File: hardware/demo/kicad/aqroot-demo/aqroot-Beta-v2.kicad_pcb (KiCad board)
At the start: 6 copper layers, 72 x 148 mm, 311 parts, among them J1 FH69-50S-0.5SH, J2 Molex_5025700893, J3 USB_C_Receptacle_USB2.0_16P, J4 JST-PH-2 BATTERY, J5 COMMUNITY_PORT_1x24, J6 JST-PH-2 SPEAKER, J7 BM02B-ACHSS-GAN-ETF, J8 QWIIC_STEMMA_QT, Q1 AO3400A, Q10 2N7002, Q2 NTMD4820N, Q3 NTMD4820N, Q4 BSS138, Q5 AO3401A, Q6 BSS138, Q7 BSS138, Q8 BSS138, Q9 BSS138, SW1 BOOT, SW2 UP, SW3 DOWN, SW4 LEFT, SW5 RIGHT, SW6 A_SELECT, SW7 B_BACK, SW9 SW_SPDT, U1 ESP32-S3-WROOM-1, U10 USBLC6-2SC6, U11 BQ25185, U12 TPS63020, U13 TPS61023, U14 MAX17048, U16 TCA4307DGKR, U17 TPS61169DCKR, U18 LTC4368-1, U19 TLV7032, U2 PCAL9535APW, U20 TPS22950C, U21 TPS61023, U22 TPS22950C, U3 PCAL9535APW, U4 BMI270, U5 MAX98357A, U6 TSOP38238, U7 E07-400M10S, U8 E22-900M22S, U9 ST25R3916-AQET, Y1 27.12MHz 10pF 3225-4P

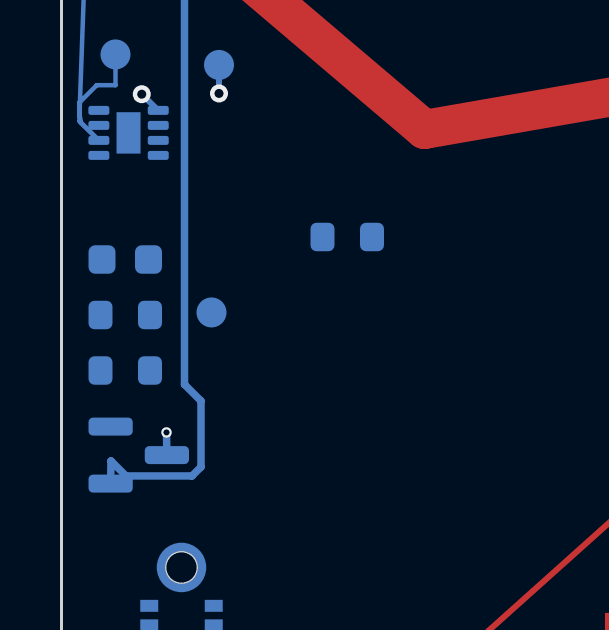
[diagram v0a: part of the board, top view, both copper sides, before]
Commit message: demo: route VBUS present tree
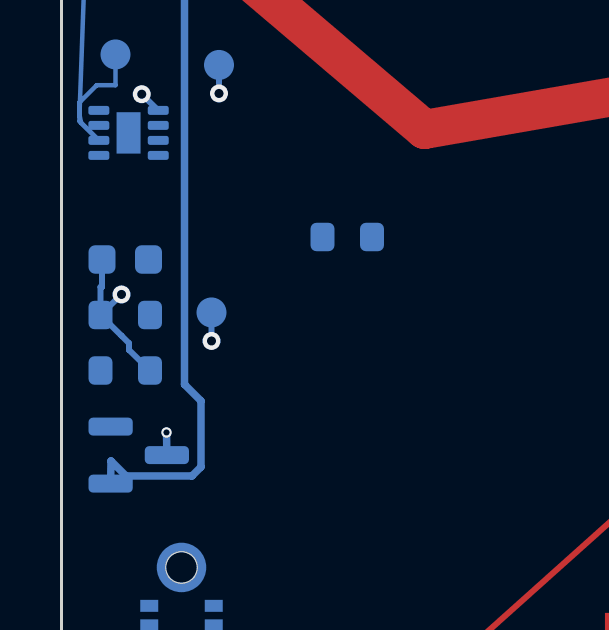
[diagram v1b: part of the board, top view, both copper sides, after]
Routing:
- net /01_POWER_TREE/VBUS_PRESENT: track 0.00 -> 10.0 mm, vias 0 -> 2
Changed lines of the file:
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@@
 		(net "/01_POWER_TREE/BAT_MID")
+	)
+	(via
+		(at 2 87.9)
+		(size 0.6)
+		(drill 0.3)
+		(layers "F.Cu" "B.Cu")
+		(net "/01_POWER_TREE/VBUS_PRESENT")
+	)
+	(via
+		(at 5 89.45)
+		(size 0.6)
+		(drill 0.3)
+		(layers "F.Cu" "B.Cu")
+		(net "/01_POWER_TREE/VBUS_PRESENT")
+	)
+	(segment
+		(start 1.3 88.585)
+		(end 1.3 87.65)
+		(width 0.2)
+		(layer "B.Cu")
+		(net "/01_POWER_TREE/VBUS_PRESENT")
+	)
+	(segment
+		(start 1.3 88.585)
+		(end 2 89.275)
+		(width 0.2)
+		(layer "B.Cu")
+		(net "/01_POWER_TREE/VBUS_PRESENT")
+	)
+	(segment
+		(start 2.25 89.525)
+		(end 2.25 89.75)
+		(width 0.2)
+		(layer "B.Cu")
+		(net "/01_POWER_TREE/VBUS_PRESENT")
+	)
+	(segment
+		(start 1.3 88.585)
+		(end 2 87.9)
+		(width 0.2)
+		(layer "B.Cu")
+		(net "/01_POWER_TREE/VBUS_PRESENT")
+	)
+	(segment
+		(start 1.3 87.65)
+		(end 1.35 87.65)
+		(width 0.2)
+		(layer "B.Cu")
+		(net "/01_POWER_TREE/VBUS_PRESENT")
+	)
+	(segment
+		(start 1.35 86.735)
+		(end 1.35 87.65)
+		(width 0.2)
+		(layer "B.Cu")
+		(net "/01_POWER_TREE/VBUS_PRESENT")
+	)
+	(segment
+		(start 2 89.275)
+		(end 2.25 89.525)
+		(width 0.2)
+		(layer "B.Cu")
+		(net "/01_POWER_TREE/VBUS_PRESENT")
+	)
+	(segment
+		(start 2.95 90.435)
+		(end 2.25 89.75)
+		(width 0.2)
+		(layer "B.Cu")
+		(net "/01_POWER_TREE/VBUS_PRESENT")
+	)
+	(segment
+		(start 5 88.5)
+		(end 5 89.45)
+		(width 0.2)
+		(layer "B.Cu")
+		(net "/01_POWER_TREE/VBUS_PRESENT")
+	)
+	(segment
+		(start 5 89.45)
+		(end 3.45 87.9)
+		(width 0.2)
+		(layer "In3.Cu")
+		(net "/01_POWER_TREE/VBUS_PRESENT")
+	)
+	(segment
+		(start 3.45 87.9)
+		(end 2 87.9)
+		(width 0.2)
+		(layer "In3.Cu")
+		(net "/01_POWER_TREE/VBUS_PRESENT")
 	)
 	(segment

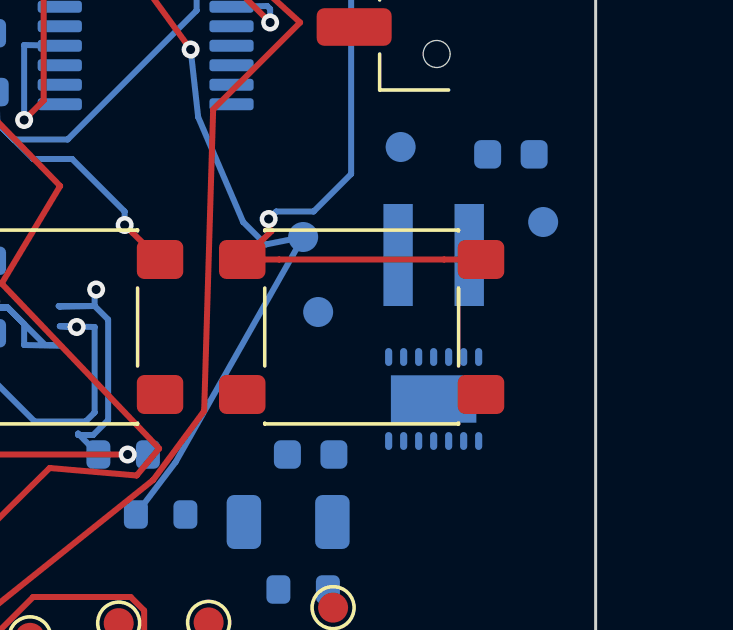
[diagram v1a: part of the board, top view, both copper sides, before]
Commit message: demo: route U12 buck-boost switch pair
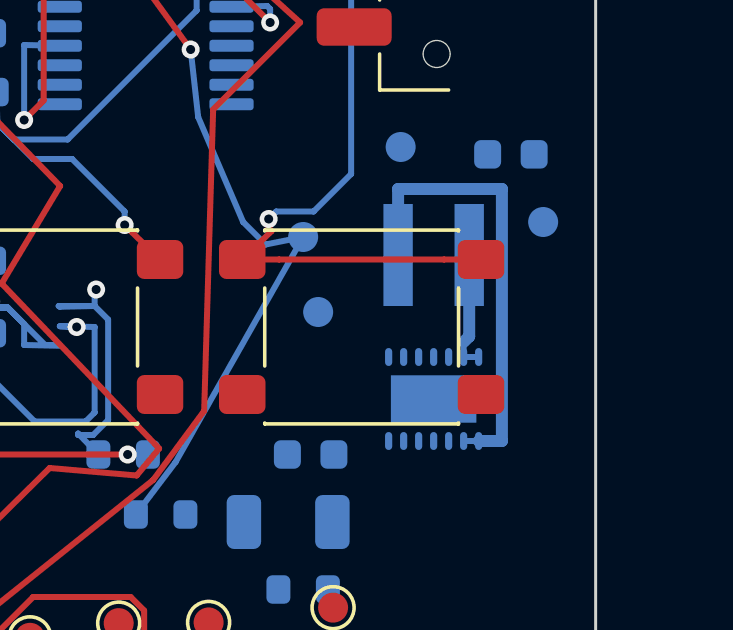
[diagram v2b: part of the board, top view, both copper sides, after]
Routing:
- net Net-(L1-Pad1): track 0.00 -> 15.3 mm
- net Net-(L1-Pad2): track 0.00 -> 3.98 mm
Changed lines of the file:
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@@
 		(net "/01_POWER_TREE/REC_DIODE_IN")
+	)
+	(segment
+		(start 67.6 100)
+		(end 67.6 99.5)
+		(width 0.2)
+		(layer "B.Cu")
+		(net "Net-(L1-Pad2)")
+	)
+	(segment
+		(start 67.785 99.315)
+		(end 67.785 96.6)
+		(width 0.4)
+		(layer "B.Cu")
+		(net "Net-(L1-Pad2)")
+	)
+	(segment
+		(start 67.6 99.5)
+		(end 67.785 99.315)
+		(width 0.4)
+		(layer "B.Cu")
+		(net "Net-(L1-Pad2)")
+	)
+	(segment
+		(start 67.6 100)
+		(end 68.1 100)
+		(width 0.2)
+		(layer "B.Cu")
+		(net "Net-(L1-Pad2)")
+	)
+	(segment
+		(start 68.875 102.8)
+		(end 68.875 94.4)
+		(width 0.4)
+		(layer "B.Cu")
+		(net "Net-(L1-Pad1)")
+	)
+	(segment
+		(start 65.415 94.4)
+		(end 65.415 96.6)
+		(width 0.4)
+		(layer "B.Cu")
+		(net "Net-(L1-Pad1)")
+	)
+	(segment
+		(start 68.1 102.8)
+		(end 68.875 102.8)
+		(width 0.4)
+		(layer "B.Cu")
+		(net "Net-(L1-Pad1)")
+	)
+	(segment
+		(start 68.875 94.4)
+		(end 65.415 94.4)
+		(width 0.4)
+		(layer "B.Cu")
+		(net "Net-(L1-Pad1)")
+	)
+	(segment
+		(start 67.6 102.8)
+		(end 68.1 102.8)
+		(width 0.2)
+		(layer "B.Cu")
+		(net "Net-(L1-Pad1)")
 	)
 	(via

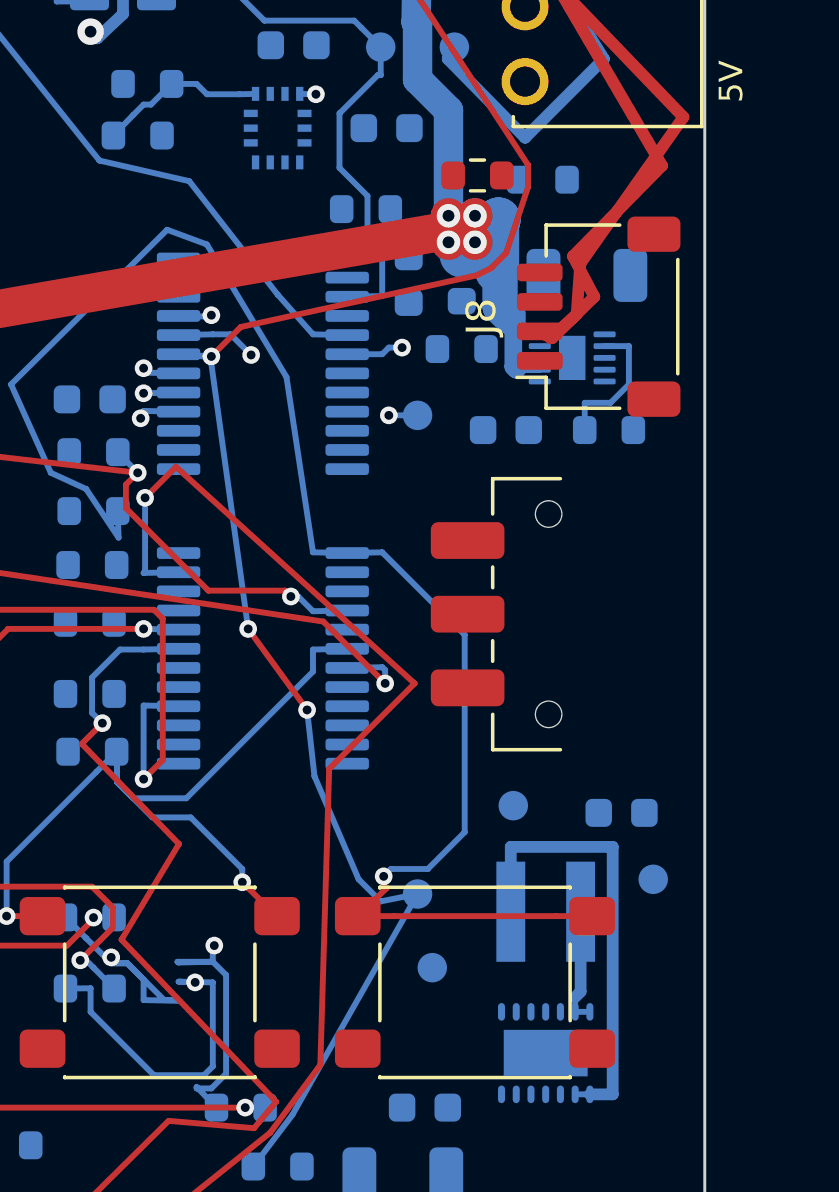
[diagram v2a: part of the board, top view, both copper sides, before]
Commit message: demo: route buck-boost feedback tree
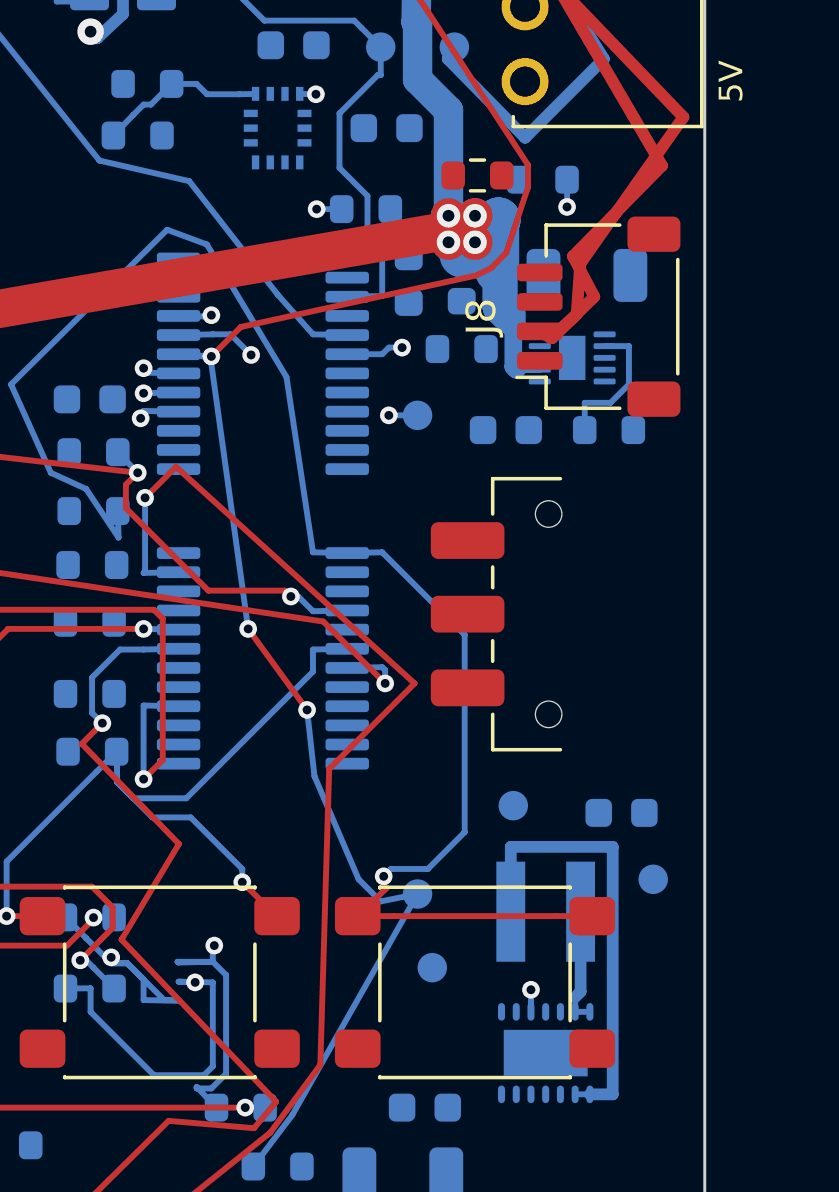
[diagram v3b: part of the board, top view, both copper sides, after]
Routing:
- net /01_POWER_TREE/V3V3_FB: track 0.00 -> 61.3 mm, vias 0 -> 3
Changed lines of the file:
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@@
 		(net "/01_POWER_TREE/REC_DIODE_IN")
+	)
+	(via
+		(at 58.825 72.75)
+		(size 0.6)
+		(drill 0.3)
+		(layers "F.Cu" "B.Cu")
+		(net "/01_POWER_TREE/V3V3_FB")
+	)
+	(via
+		(at 67.325 72.675)
+		(size 0.6)
+		(drill 0.3)
+		(layers "F.Cu" "B.Cu")
+		(net "/01_POWER_TREE/V3V3_FB")
+	)
+	(via
+		(at 66.1 99.25)
+		(size 0.6)
+		(drill 0.3)
+		(layers "F.Cu" "B.Cu")
+		(net "/01_POWER_TREE/V3V3_FB")
+	)
+	(segment
+		(start 66.1 100)
+		(end 66.1 99.25)
+		(width 0.2)
+		(layer "B.Cu")
+		(net "/01_POWER_TREE/V3V3_FB")
+	)
+	(segment
+		(start 66.1 100)
+		(end 66.1 99.25)
+		(width 0.2)
+		(layer "B.Cu")
+		(net "/01_POWER_TREE/V3V3_FB")
+	)
+	(segment
+		(start 67.325 71.75)
+		(end 67.325 72.675)
+		(width 0.2)
+		(layer "B.Cu")
+		(net "/01_POWER_TREE/V3V3_FB")
+	)
+	(segment
+		(start 59.675 72.75)
+		(end 58.825 72.75)
+		(width 0.2)
+		(layer "B.Cu")
+		(net "/01_POWER_TREE/V3V3_FB")
+	)
+	(segment
+		(start 56 75.575)
+		(end 58.825 72.75)
+		(width 0.2)
+		(layer "In2.Cu")
+		(net "/01_POWER_TREE/V3V3_FB")
+	)
+	(segment
+		(start 66.1 99.25)
+		(end 59.975 84.3)
+		(width 0.2)
+		(layer "In2.Cu")
+		(net "/01_POWER_TREE/V3V3_FB")
+	)
+	(segment
+		(start 55.975 77.925)
+		(end 56 75.575)
+		(width 0.2)
+		(layer "In2.Cu")
+		(net "/01_POWER_TREE/V3V3_FB")
+	)
+	(segment
+		(start 59.975 84.3)
+		(end 55.975 77.925)
+		(width 0.2)
+		(layer "In2.Cu")
+		(net "/01_POWER_TREE/V3V3_FB")
+	)
+	(segment
+		(start 66.1 99.25)
+		(end 70.075 75.425)
+		(width 0.2)
+		(layer "In3.Cu")
+		(net "/01_POWER_TREE/V3V3_FB")
+	)
+	(segment
+		(start 70.075 75.425)
+		(end 67.325 72.675)
+		(width 0.2)
+		(layer "In3.Cu")
+		(net "/01_POWER_TREE/V3V3_FB")
 	)
 	(segment

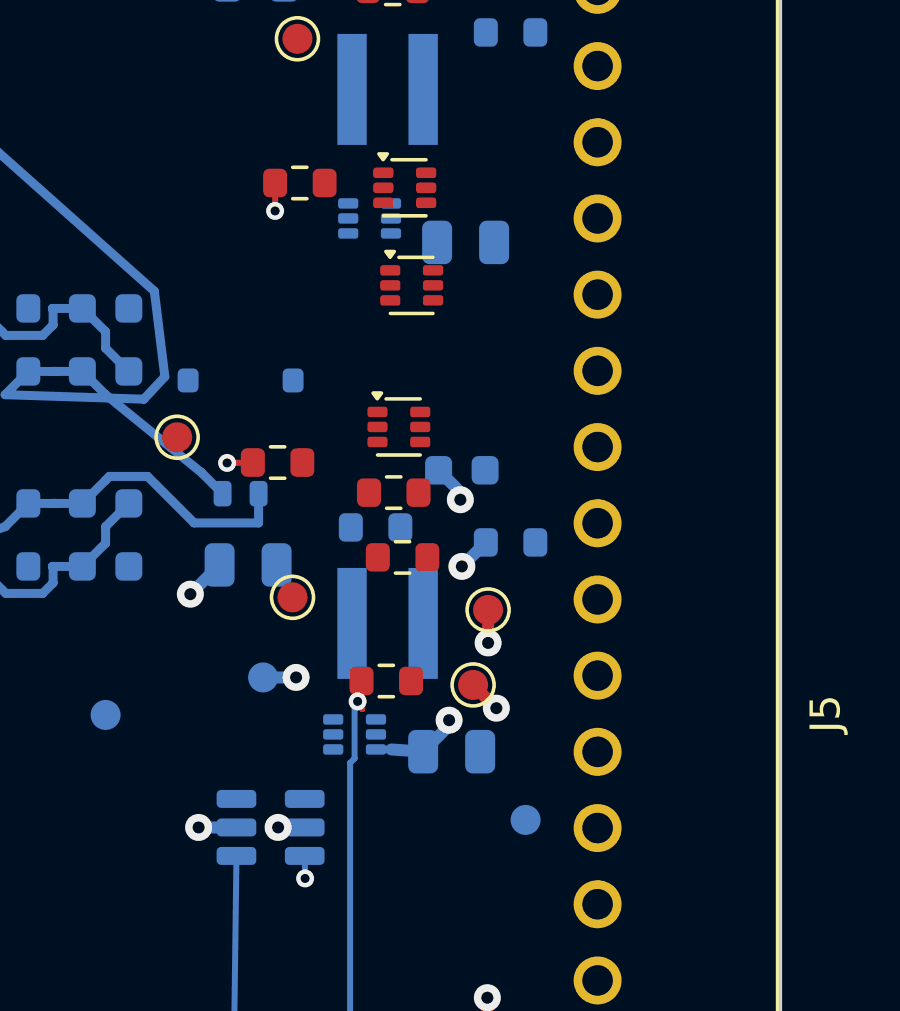
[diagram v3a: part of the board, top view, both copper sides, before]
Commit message: demo: route retained XGPIO header pair
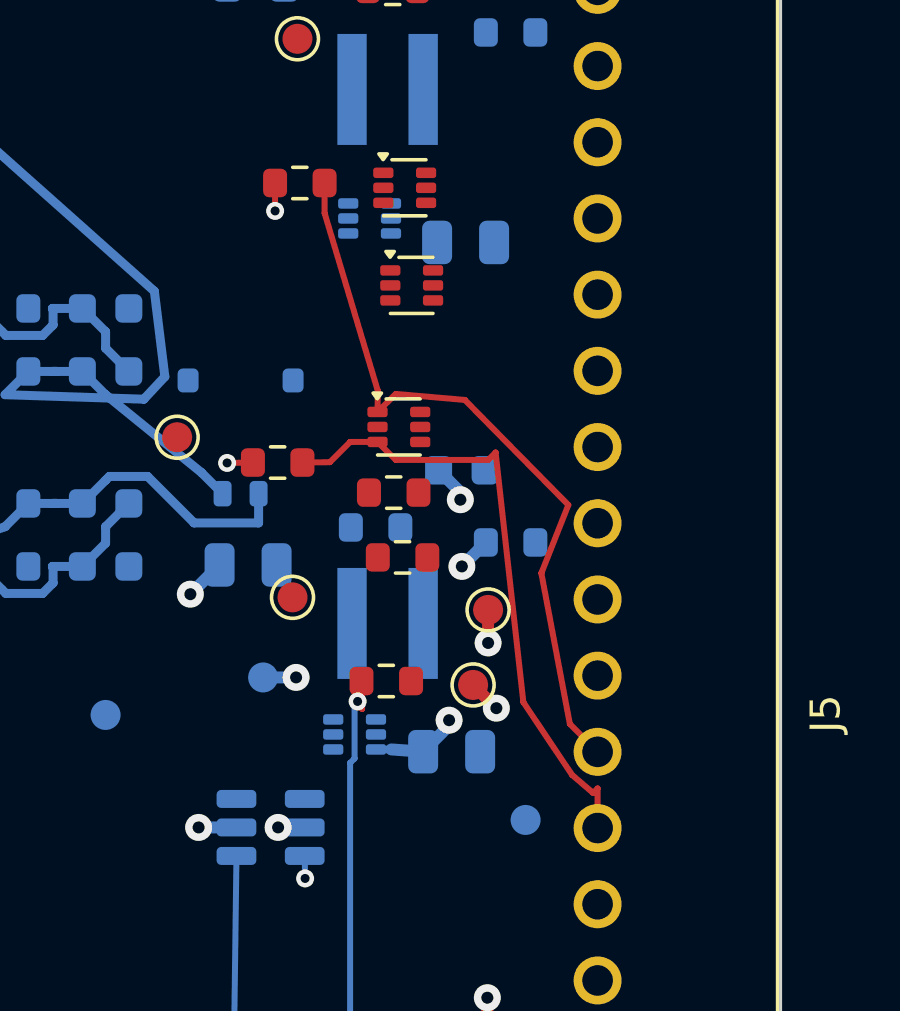
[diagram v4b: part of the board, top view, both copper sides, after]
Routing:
- net /09_COMMUNITY_HEADER/XGPIO4_HDR: track 0.00 -> 24.8 mm
- net /09_COMMUNITY_HEADER/XGPIO5_HDR: track 0.00 -> 20.8 mm
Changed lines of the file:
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@@
+	)
+	(segment
+		(start 65.9 40.48)
+		(end 64.975 39.55)
+		(width 0.2)
+		(layer "F.Cu")
+		(net "/09_COMMUNITY_HEADER/XGPIO4_HDR")
+	)
+	(segment
+		(start 56.799309 21.51856)
+		(end 56.8 22.525)
+		(width 0.2)
+		(layer "F.Cu")
+		(net "/09_COMMUNITY_HEADER/XGPIO4_HDR")
+	)
+	(segment
+		(start 58.563109 29.150496)
+		(end 59.175 28.55)
+		(width 0.2)
+		(layer "F.Cu")
+		(net "/09_COMMUNITY_HEADER/XGPIO4_HDR")
+	)
+	(segment
+		(start 56.8 22.525)
+		(end 58.575 28.45)
+		(width 0.2)
+		(layer "F.Cu")
+		(net "/09_COMMUNITY_HEADER/XGPIO4_HDR")
+	)
+	(segment
+		(start 58.563109 29.150496)
+		(end 58.575 28.45)
+		(width 0.2)
+		(layer "F.Cu")
+		(net "/09_COMMUNITY_HEADER/XGPIO4_HDR")
+	)
+	(segment
+		(start 64.025 34.525)
+		(end 64.975 39.55)
+		(width 0.2)
+		(layer "F.Cu")
+		(net "/09_COMMUNITY_HEADER/XGPIO4_HDR")
+	)
+	(segment
+		(start 64.925 32.25)
+		(end 64.025 34.525)
+		(width 0.2)
+		(layer "F.Cu")
+		(net "/09_COMMUNITY_HEADER/XGPIO4_HDR")
+	)
+	(segment
+		(start 59.175 28.55)
+		(end 61.475 28.75)
+		(width 0.2)
+		(layer "F.Cu")
+		(net "/09_COMMUNITY_HEADER/XGPIO4_HDR")
+	)
+	(segment
+		(start 61.475 28.75)
+		(end 64.925 32.25)
+		(width 0.2)
+		(layer "F.Cu")
+		(net "/09_COMMUNITY_HEADER/XGPIO4_HDR")
+	)
+	(segment
+		(start 56.975 30.825)
+		(end 57.65 30.15)
+		(width 0.2)
+		(layer "F.Cu")
+		(net "/09_COMMUNITY_HEADER/XGPIO5_HDR")
+	)
+	(segment
+		(start 63.425 38.825)
+		(end 65.05 41.25)
+		(width 0.2)
+		(layer "F.Cu")
+		(net "/09_COMMUNITY_HEADER/XGPIO5_HDR")
+	)
+	(segment
+		(start 58.563109 30.150496)
+		(end 57.7 30.15)
+		(width 0.2)
+		(layer "F.Cu")
+		(net "/09_COMMUNITY_HEADER/XGPIO5_HDR")
+	)
+	(segment
+		(start 57.65 30.15)
+		(end 57.7 30.15)
+		(width 0.2)
+		(layer "F.Cu")
+		(net "/09_COMMUNITY_HEADER/XGPIO5_HDR")
+	)
+	(segment
+		(start 65.05 41.25)
+		(end 65.75 41.85)
+		(width 0.2)
+		(layer "F.Cu")
+		(net "/09_COMMUNITY_HEADER/XGPIO5_HDR")
+	)
+	(segment
+		(start 65.9 43.02)
+		(end 65.9 41.7)
+		(width 0.2)
+		(layer "F.Cu")
+		(net "/09_COMMUNITY_HEADER/XGPIO5_HDR")
+	)
+	(segment
+		(start 65.75 41.85)
+		(end 65.9 41.7)
+		(width 0.2)
+		(layer "F.Cu")
+		(net "/09_COMMUNITY_HEADER/XGPIO5_HDR")
+	)
+	(segment
+		(start 62.5 30.5)
+		(end 63.425 38.825)
+		(width 0.2)
+		(layer "F.Cu")
+		(net "/09_COMMUNITY_HEADER/XGPIO5_HDR")
+	)
+	(segment
+		(start 56.059814 30.836116)
+		(end 56.975 30.825)
+		(width 0.2)
+		(layer "F.Cu")
+		(net "/09_COMMUNITY_HEADER/XGPIO5_HDR")
+	)
+	(segment
+		(start 59.175 30.75)
+		(end 62.25 30.75)
+		(width 0.2)
+		(layer "F.Cu")
+		(net "/09_COMMUNITY_HEADER/XGPIO5_HDR")
+	)
+	(segment
+		(start 58.563109 30.150496)
+		(end 59.175 30.75)
+		(width 0.2)
+		(layer "F.Cu")
+		(net "/09_COMMUNITY_HEADER/XGPIO5_HDR")
+	)
+	(segment
+		(start 62.25 30.75)
+		(end 62.5 30.5)
+		(width 0.2)
+		(layer "F.Cu")
+		(net "/09_COMMUNITY_HEADER/XGPIO5_HDR")
 	)
 	(segment

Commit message: demo: route accessory 5V current limit
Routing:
- net /01_POWER_TREE/ACC_5V_ILIM: track 0.00 -> 42.4 mm
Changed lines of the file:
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@@
 		(net "/ACC_5V_SW_EN")
+	)
+	(segment
+		(start 34.375 47.15)
+		(end 24.975 56.55)
+		(width 0.2)
+		(layer "B.Cu")
+		(net "/01_POWER_TREE/ACC_5V_ILIM")
+	)
+	(segment
+		(start 55.025 42.05)
+		(end 54.725 41.55)
+		(width 0.2)
+		(layer "B.Cu")
+		(net "/01_POWER_TREE/ACC_5V_ILIM")
+	)
+	(segment
+		(start 24.282189 57.258894)
+		(end 24.975 56.55)
+		(width 0.2)
+		(layer "B.Cu")
+		(net "/01_POWER_TREE/ACC_5V_ILIM")
+	)
+	(segment
+		(start 56.1375 42.05)
+		(end 55.025 42.05)
+		(width 0.2)
+		(layer "B.Cu")
+		(net "/01_POWER_TREE/ACC_5V_ILIM")
+	)
+	(segment
+		(start 46.575 36.4)
+		(end 35.45 47.45)
+		(width 0.2)
+		(layer "B.Cu")
+		(net "/01_POWER_TREE/ACC_5V_ILIM")
+	)
+	(segment
+		(start 54.725 41.55)
+		(end 46.575 36.4)
+		(width 0.2)
+		(layer "B.Cu")
+		(net "/01_POWER_TREE/ACC_5V_ILIM")
+	)
+	(segment
+		(start 35.45 47.45)
+		(end 34.375 47.15)
+		(width 0.2)
+		(layer "B.Cu")
+		(net "/01_POWER_TREE/ACC_5V_ILIM")
 	)
 	(via

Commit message: demo: route backlight switch node
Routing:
- net /03_SPI_A_DISPLAY_SD/BL_SW: track 0.00 -> 16.2 mm
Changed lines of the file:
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@@
+	)
+	(segment
+		(start 1.3625 123.25)
+		(end 1.35 123.975)
+		(width 0.4)
+		(layer "B.Cu")
+		(net "/03_SPI_A_DISPLAY_SD/BL_SW")
+	)
+	(segment
+		(start 5.425 119.1)
+		(end 5.225 118.9)
+		(width 0.4)
+		(layer "B.Cu")
+		(net "/03_SPI_A_DISPLAY_SD/BL_SW")
+	)
+	(segment
+		(start 4.185 118.9)
+		(end 5.225 118.9)
+		(width 0.4)
+		(layer "B.Cu")
+		(net "/03_SPI_A_DISPLAY_SD/BL_SW")
+	)
+	(segment
+		(start 5.425 123.125)
+		(end 5.425 119.1)
+		(width 0.4)
+		(layer "B.Cu")
+		(net "/03_SPI_A_DISPLAY_SD/BL_SW")
+	)
+	(segment
+		(start 7.65 121.325)
+		(end 7.65 122.75)
+		(width 0.4)
+		(layer "B.Cu")
+		(net "/03_SPI_A_DISPLAY_SD/BL_SW")
+	)
+	(segment
+		(start 6.8 122.75)
+		(end 7.65 122.75)
+		(width 0.4)
+		(layer "B.Cu")
+		(net "/03_SPI_A_DISPLAY_SD/BL_SW")
+	)
+	(segment
+		(start 5.225 118.9)
+		(end 7.65 121.325)
+		(width 0.4)
+		(layer "B.Cu")
+		(net "/03_SPI_A_DISPLAY_SD/BL_SW")
+	)
+	(segment
+		(start 4.575 123.975)
+		(end 5.425 123.125)
+		(width 0.4)
+		(layer "B.Cu")
+		(net "/03_SPI_A_DISPLAY_SD/BL_SW")
+	)
+	(segment
+		(start 1.35 123.975)
+		(end 4.575 123.975)
+		(width 0.4)
+		(layer "B.Cu")
+		(net "/03_SPI_A_DISPLAY_SD/BL_SW")
 	)
 	(segment
